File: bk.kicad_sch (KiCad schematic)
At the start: 200 parts, among them J5 Conn_01x09, J6 Screw_Terminal_01x02, J7 Conn_01x02, J8 Conn_02x04, Q22 CSD13380F3, Q23 CSD13380F3, Q24 CSD13380F3, Q25 CSD13380F3, Q26 CSD13380F3, Q27 CSD13380F3, Q28 CSD13380F3, Q29 CSD13380F3, Q30 Q_NPN, Q31 Q_NMOS, Q32 Q_PMOS, Q33 Q_NMOS, Q34 2N7002E, Q35 2N7002E, Q36 TP0610K, Q37 Q_NMOS, Q38 Q_NMOS, Q39 Q_PMOS, Q40 Q_NMOS, Q41 Q_NMOS, Q42 Q_PMOS, SW2 SW_Push, U10 TPS3839DBZ, U6 BQ7693000DBT, U7 LMT01LPG, U8 MSP430G2553IPW20, U9 BQ76200PW

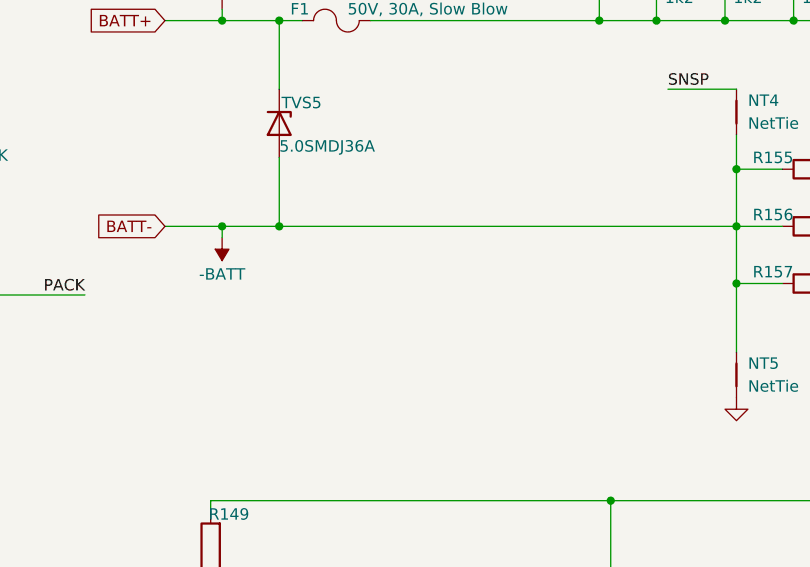
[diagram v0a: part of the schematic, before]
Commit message: cgr, dsg fets + jtag
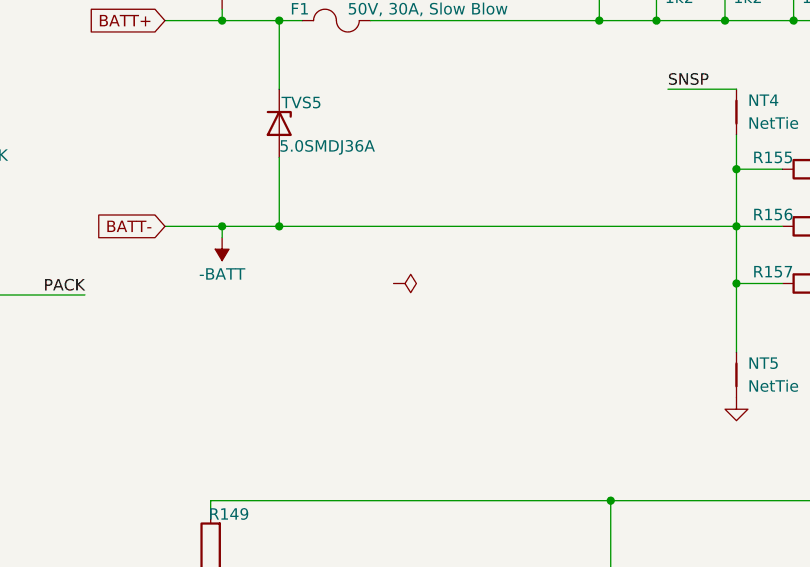
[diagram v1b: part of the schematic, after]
